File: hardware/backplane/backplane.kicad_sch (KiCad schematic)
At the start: 84 parts, among them J1 Bus_PCI_Express_x1, J2 PWR, J3 Bus_PCI_Express_x1, J4 Bus_PCI_Express_x1, J5 Bus_PCI_Express_x1, J6 Bus_PCI_Express_x1, J7 Bus_PCI_Express_x1, J8 Bus_PCI_Express_x1, M1 FAN1, Q1 IRFS7530TRL7PP, Q2 AO3400A, U1 AP64352SP-13, U2 TCA9548APWR, U3 TCA9539PWR, U4 LM74700

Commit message: chore: update 3d models for rendering
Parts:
- F1: LCSC (none) -> C207061
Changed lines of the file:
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@@
+			)
+		)
+		(property "LCSC" "C207061"
+			(at 97.79 29.21 90)
+			(hide yes)
+			(show_name no)
+			(do_not_autoplace no)
+			(effects
+				(font
+					(size 1.27 1.27)
+				)
 			)
 		)

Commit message: fix(backplane): switch TVS diode to bidirectional
feat(backplane): swap fan FET for higher voltage spec
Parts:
- D1: value SMCJ33A -> SMCJ33CA; LCSC C42371548 -> C310048
- Q2: value AO3400A -> IRLML0060TRPbF; LCSC C20917 -> C67274
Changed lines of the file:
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@@
 			)
 		)
-		(property "Value" "SMCJ33A"
+		(property "Value" "SMCJ33CA"
 			(at 100.33 35.5599 90)
 			(show_name no)
@@
 			)
 		)
-		(property "LCSC" "C42371548"
+		(property "LCSC" "C310048"
 			(at 102.87 34.29 90)
 			(hide yes)
@@
 			)
 		)
-		(property "Value" "AO3400A"
+		(property "Value" "IRLML0060TRPbF"
 			(at 200.66 46.9899 0)
 			(show_name no)
@@
 			)
 		)
-		(property "Datasheet" "http://www.aosmd.com/pdfs/datasheet/AO3400A.pdf"
+		(property "Datasheet" "https://www.infineon.com/assets/row/public/documents/24/49/infineon-irlml0060-datasheet-en.pdf"
 			(at 199.39 49.53 0)
 			(hide yes)
@@
 			)
 		)
-		(property "Description" "30V Vds, 5.7A Id, N-Channel MOSFET, SOT-23"
+		(property "Description" "60V Vds, 2.7A Id, N-Channel MOSFET, SOT-23"
 			(at 194.31 45.72 0)
 			(hide yes)
@@
 			)
 		)
-		(property "LCSC" "C20917"
+		(property "LCSC" "C67274"
 			(at 194.31 45.72 0)
 			(hide yes)

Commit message: fix(backplane): switch fan from VIN to 5V supply
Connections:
- net +5V: now also D3.1 (K), M1.2 (+)
- net VIN: no longer D3.1 (K), M1.2 (+)
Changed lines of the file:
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@@
 	)
 	(junction
-		(at 196.85 26.67)
-		(diameter 0)
-		(color 0 0 0 0)
-	)
-	(junction
 		(at 189.23 229.87)
 		(diameter 0)
@@
 	)
 	(junction
+		(at 196.85 26.67)
+		(diameter 0)
+		(color 0 0 0 0)
+	)
+	(junction
 		(at 64.77 227.33)
 		(diameter 0)
@@
 	(wire
 		(pts
-			(xy 193.04 22.86) (xy 196.85 22.86)
-		)
-		(stroke
-			(width 0)
-			(type default)
-		)
-	)
-	(wire
-		(pts
 			(xy 233.68 114.3) (xy 233.68 111.76)
 		)
@@
 	(wire
 		(pts
-			(xy 196.85 22.86) (xy 196.85 26.67)
+			(xy 196.85 24.13) (xy 196.85 26.67)
 		)
 		(stroke
@@
 	(global_label "VIN"
 		(shape input)
-		(at 193.04 22.86 180)
-		(fields_autoplaced yes)
-		(effects
-			(font
-				(size 1.27 1.27)
-			)
-			(justify right)
-		)
-		(property "Intersheetrefs" "${INTERSHEET_REFS}"
-			(at 187.0309 22.86 0)
-			(hide yes)
-			(show_name no)
-			(do_not_autoplace no)
-			(effects
-				(font
-					(size 1.27 1.27)
-				)
-				(justify right)
-			)
-		)
-	)
-	(global_label "VIN"
-		(shape input)
 		(at 316.23 72.39 180)
 		(fields_autoplaced yes)
@@
 					(unit 1)
 				)
+			)
+		)
+	)
+	(symbol
+		(lib_id "power:+5V")
+		(at 196.85 24.13 0)
+		(unit 1)
+		(body_style 1)
+		(exclude_from_sim no)
+		(in_bom yes)
+		(on_board yes)
+		(in_pos_files yes)
+		(dnp no)
+		(fields_autoplaced yes)
+		(property "Reference" "#PWR054"
+			(at 196.85 27.94 0)
+			(hide yes)
+			(show_name no)
+			(do_not_autoplace no)
+			(effects
+				(font
+					(size 1.27 1.27)
+				)
+			)
+		)
+		(property "Value" "+5V"
+			(at 196.85 19.05 0)
+			(show_name no)
+			(do_not_autoplace no)
+			(effects
+				(font
+					(size 1.27 1.27)
+				)
+			)
+		)
+		(property "Footprint" ""
+			(at 196.85 24.13 0)
+			(hide yes)
+			(show_name no)
+			(do_not_autoplace no)
+			(effects
+				(font
+					(size 1.27 1.27)
+				)
+			)
+		)
+		(property "Datasheet" ""
+			(at 196.85 24.13 0)
+			(hide yes)
+			(show_name no)
+			(do_not_autoplace no)
+			(effects
+				(font
+					(size 1.27 1.27)
+				)
+			)
+		)
+		(property "Description" "Power symbol creates a global label with name \"+5V\""
+			(at 196.85 24.13 0)
+			(hide yes)
+			(show_name no)
+			(do_not_autoplace no)
+			(effects
+				(font
+					(size 1.27 1.27)
+				)
+			)
+		)
+		(pin "1"
+		)
+		(instances
+			(project "backplane"
+				(path "/4d913069-4b50-4112-91ac-a1bdeabaace5"
+					(reference "#PWR054")
+					(unit 1)
+				)

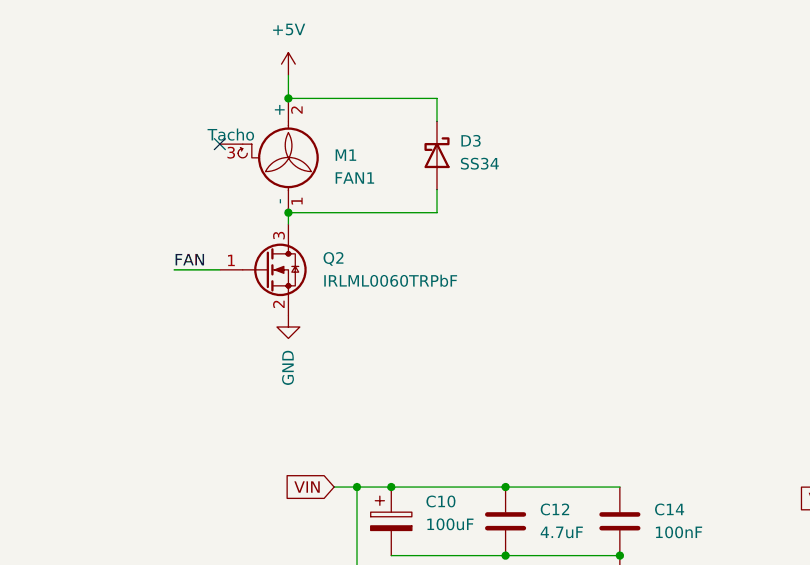
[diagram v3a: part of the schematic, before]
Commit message: fix(backplane): switch fan FET back to AO3400A
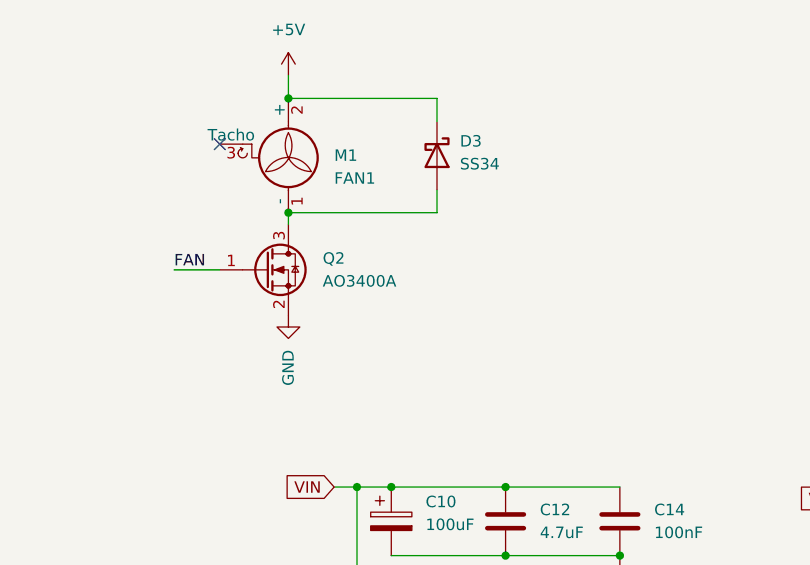
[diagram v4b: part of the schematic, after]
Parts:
- Q2: value IRLML0060TRPbF -> AO3400A; LCSC C67274 -> C20917
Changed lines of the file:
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@@
 			)
 		)
-		(property "Value" "IRLML0060TRPbF"
+		(property "Value" "AO3400A"
 			(at 200.66 46.9899 0)
 			(show_name no)
@@
 			)
 		)
-		(property "Datasheet" "https://www.infineon.com/assets/row/public/documents/24/49/infineon-irlml0060-datasheet-en.pdf"
+		(property "Datasheet" "http://www.aosmd.com/pdfs/datasheet/AO3400A.pdf"
 			(at 199.39 49.53 0)
 			(hide yes)
@@
 			)
 		)
-		(property "Description" "60V Vds, 2.7A Id, N-Channel MOSFET, SOT-23"
+		(property "Description" "30V Vds, 5.7A Id, N-Channel MOSFET, SOT-23"
 			(at 194.31 45.72 0)
 			(hide yes)
@@
 			)
 		)
-		(property "LCSC" "C67274"
+		(property "LCSC" "C20917"
 			(at 194.31 45.72 0)
 			(hide yes)
